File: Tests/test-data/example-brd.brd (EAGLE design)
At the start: 190.5 x 215.9 mm, 20 parts, among them J1 DIP16SOCKET, J2 DIP16SOCKET, U10 74LS174N, U11 74LS174N, U12 74ALS27N, U13 74LS174N, U14 74180N, U17 74LS123N, U18 SN15836N, U2 HD6821P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

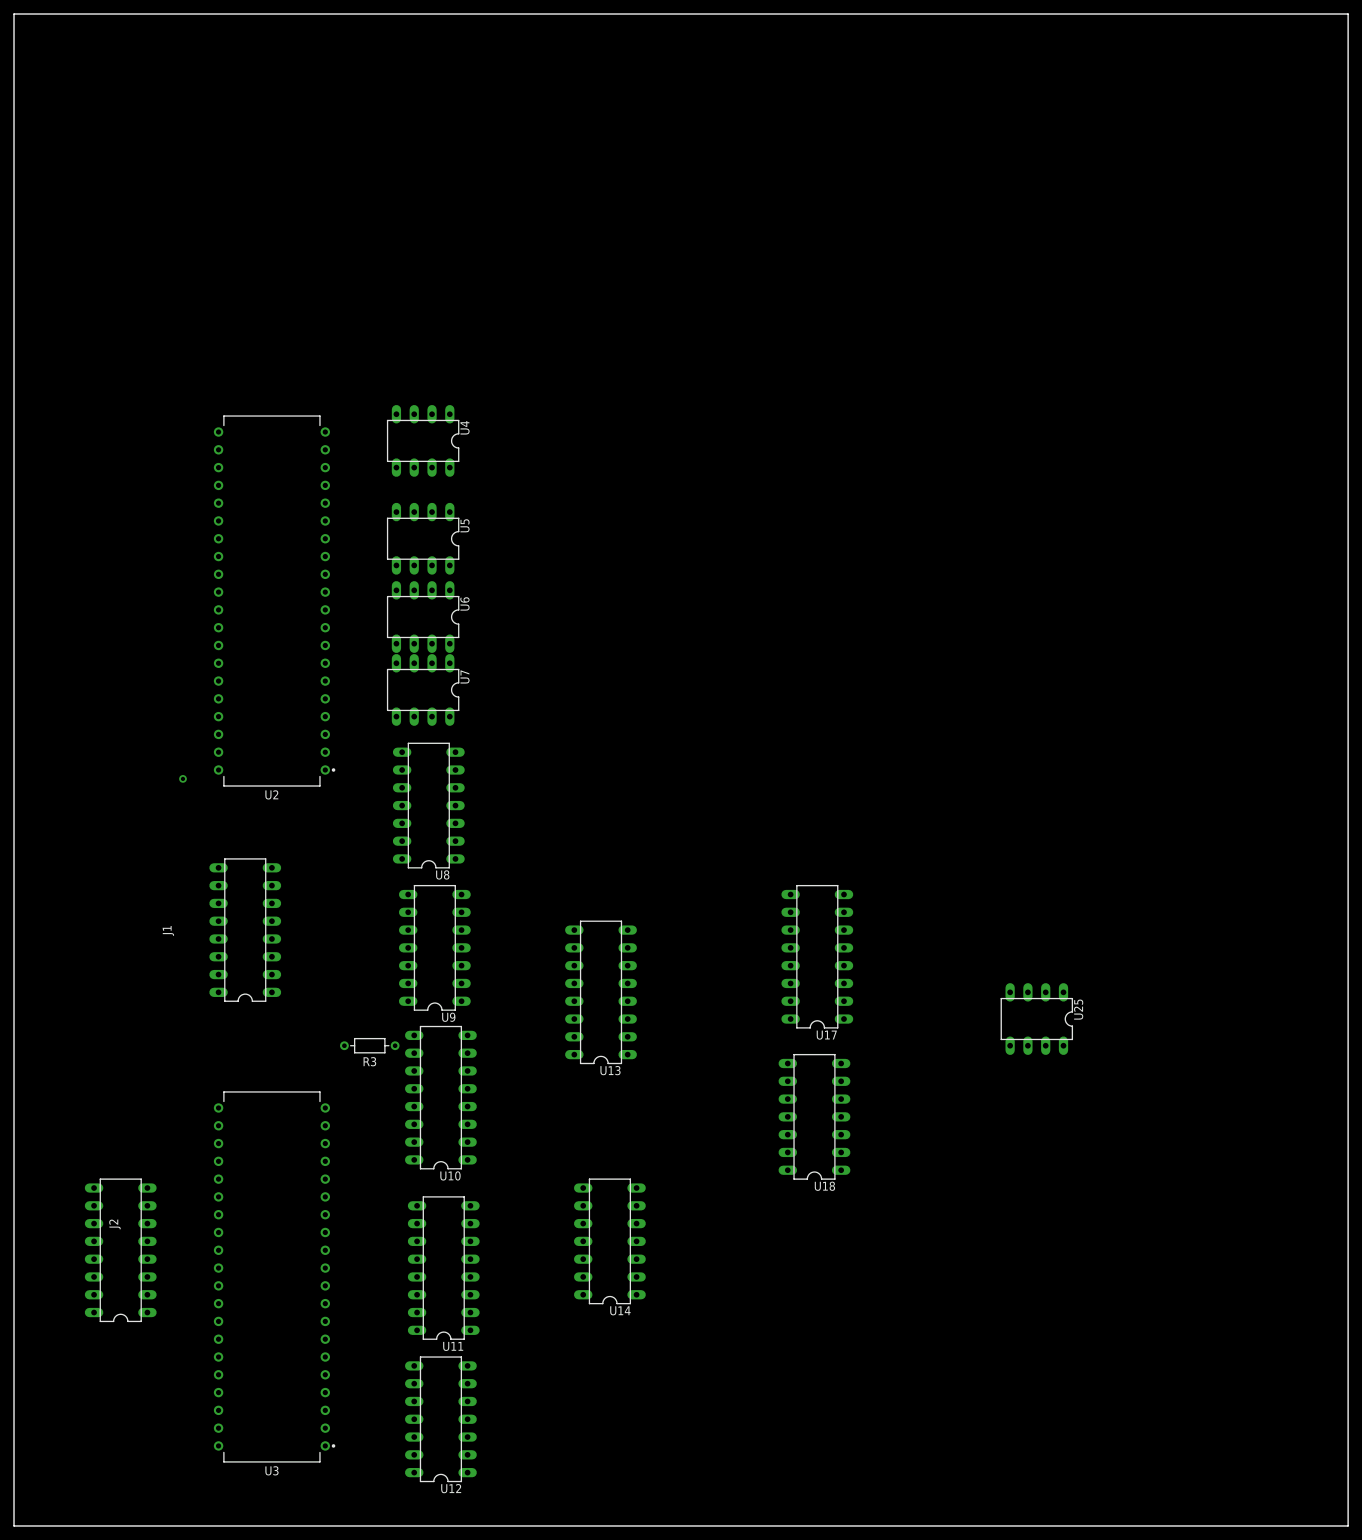
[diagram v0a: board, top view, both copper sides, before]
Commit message: Symbols and DeviceSets are now loaded
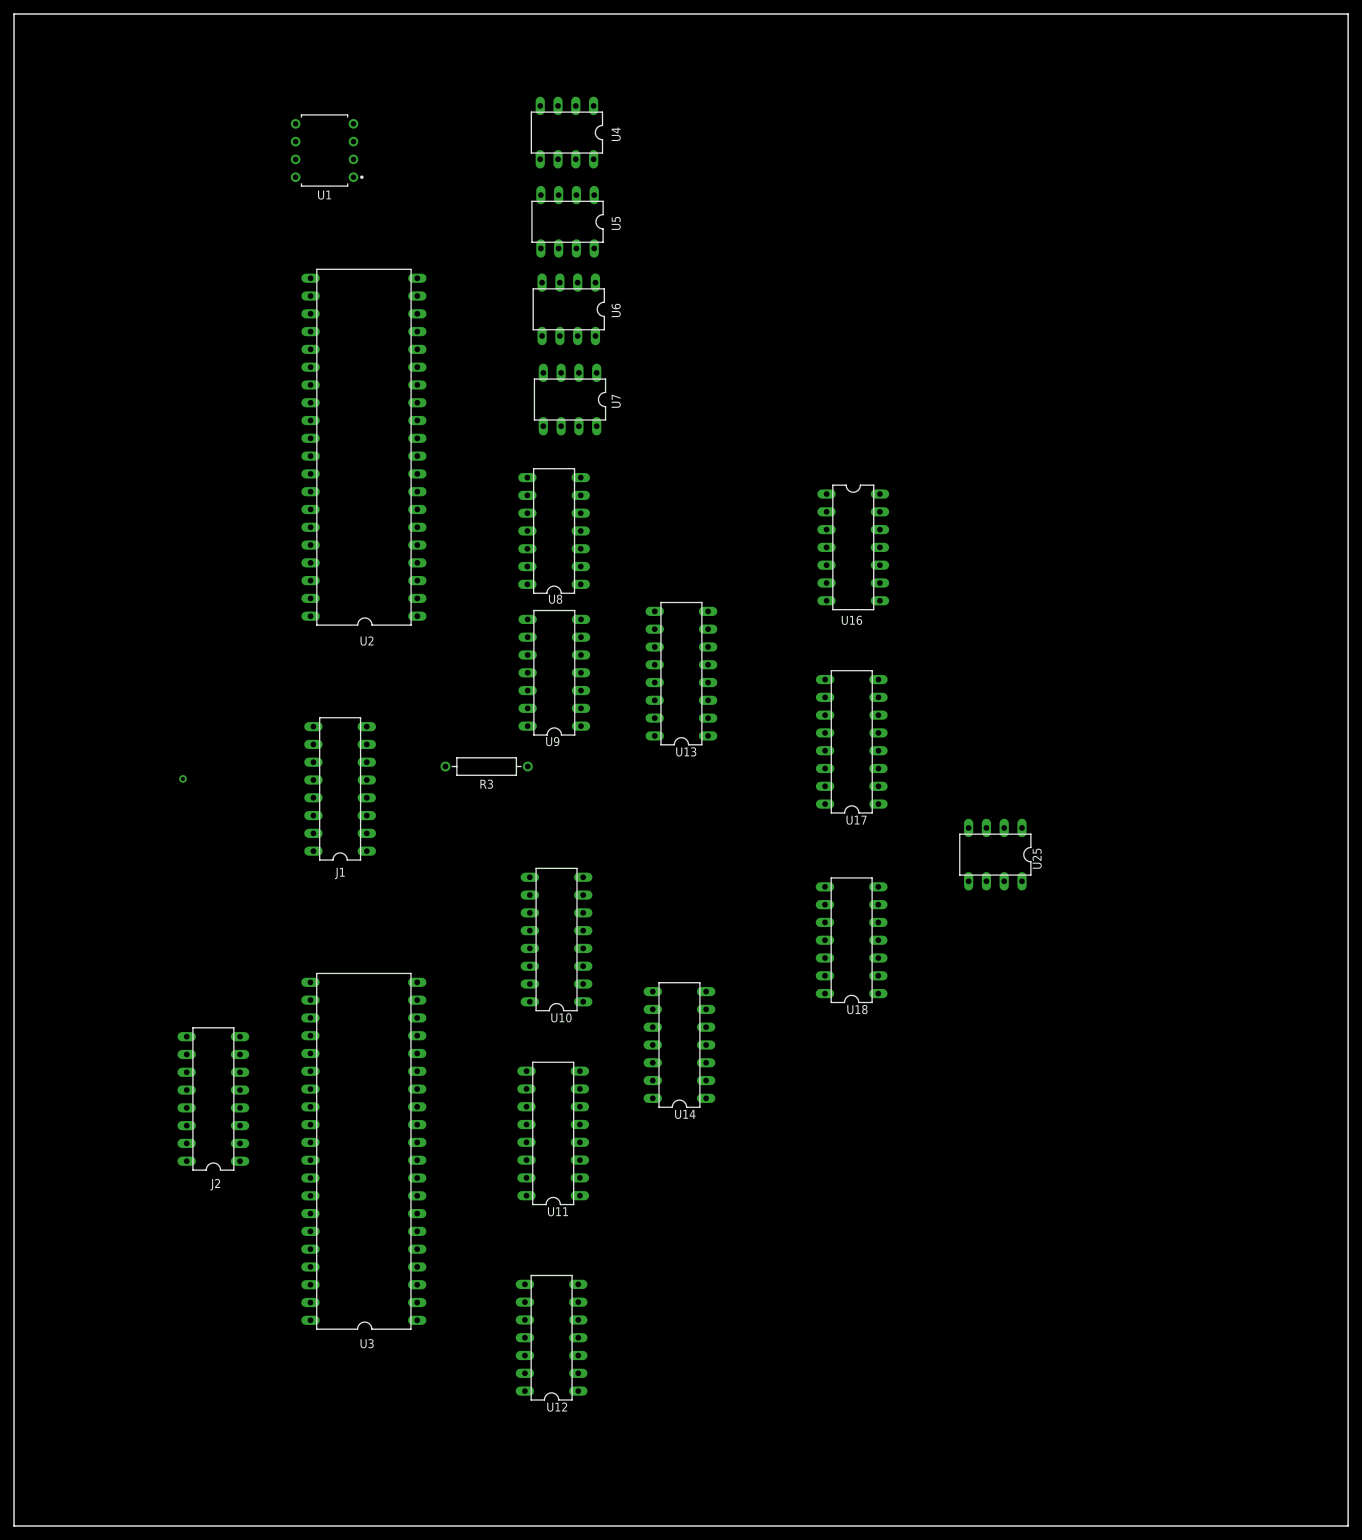
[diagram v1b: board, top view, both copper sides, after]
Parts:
- added U1: LM555_DIP, IC_Clock-Timing:DIP826W53P254L959H508Q8B
- added U16: 74180N, 74ttl-din:DIL14
- R3: device Resistor:RESAD724W46L381D178B -> Resistor:RESAD1176W63L850D250B
- U2, U3: device owen-library:DIP1524W53P254L5283H508Q40B -> owen-library:DIL40
- moved U5 49.7 mm to (79.0, 186.2)
- moved U6 48.6 mm to (79.2, 173.7)
- moved U4 48.6 mm to (79.0, 199.0)
- moved U13 46.9 mm to (95.3, 121.7)
- moved U7 46.5 mm to (79.4, 160.8)
- moved R3 43.2 mm to (67.5, 108.4)
- moved U8 43.1 mm to (77.1, 142.1)
- moved U9 42.8 mm to (77.2, 121.8)
- moved U17 31.1 mm to (119.6, 112.0)
- moved U14 29.8 mm to (95.0, 68.7)
- moved U10 28.0 mm to (77.5, 83.7)
- moved U18 25.8 mm to (119.6, 83.6)
- moved U2 25.6 mm to (50.0, 154.0), turned to 90 degrees
- moved J2 25.3 mm to (28.5, 61.0)
- moved U11 24.8 mm to (77.0, 56.1)
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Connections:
- new net V+: U1.8
- net +UB: now also U16.14
- net -UB: now also U16.7
- net GND: now also U1.1
